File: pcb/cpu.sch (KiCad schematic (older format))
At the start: 35 parts, among them P27 BDM, P57 TX1, P58 RX1, P59 TX, P60 RX, P64 CAN-RX-TX, U1 MC9S12XDP512, X1 16MHz

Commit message: Renamed RX to RX0 and TX to TX0 since there is RX1/TX1 already marked.
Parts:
- P59: value TX -> TX0
- P60: value RX -> RX0
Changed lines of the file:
@@
-EESchema Schematic File Version 2  date Thu 23 May 2013 09:58:23 PM EDT
+EESchema Schematic File Version 2  date Fri 24 May 2013 09:31:09 PM EDT
 LIBS:opto
 LIBS:power
@@
 Sheet 2 7
 Title "Jaguar PCB for FreeEMS"
-Date "24 may 2013"
+Date "25 may 2013"
 Rev "0.6-alpha"
 Comp "git hash: xxxxxxxxxx"
@@
 P 5600 1500
 F 0 "P60" H 5680 1500 40  0000 L CNN
-F 1 "RX" H 5600 1555 30  0001 C CNN
+F 1 "RX0" H 5600 1555 30  0001 C CNN
 	1    5600 1500
 	0    -1   -1   0
@@
 P 5500 1500
 F 0 "P59" H 5580 1500 40  0000 L CNN
-F 1 "TX" H 5500 1555 30  0001 C CNN
+F 1 "TX0" H 5500 1555 30  0001 C CNN
 	1    5500 1500
 	0    -1   -1   0

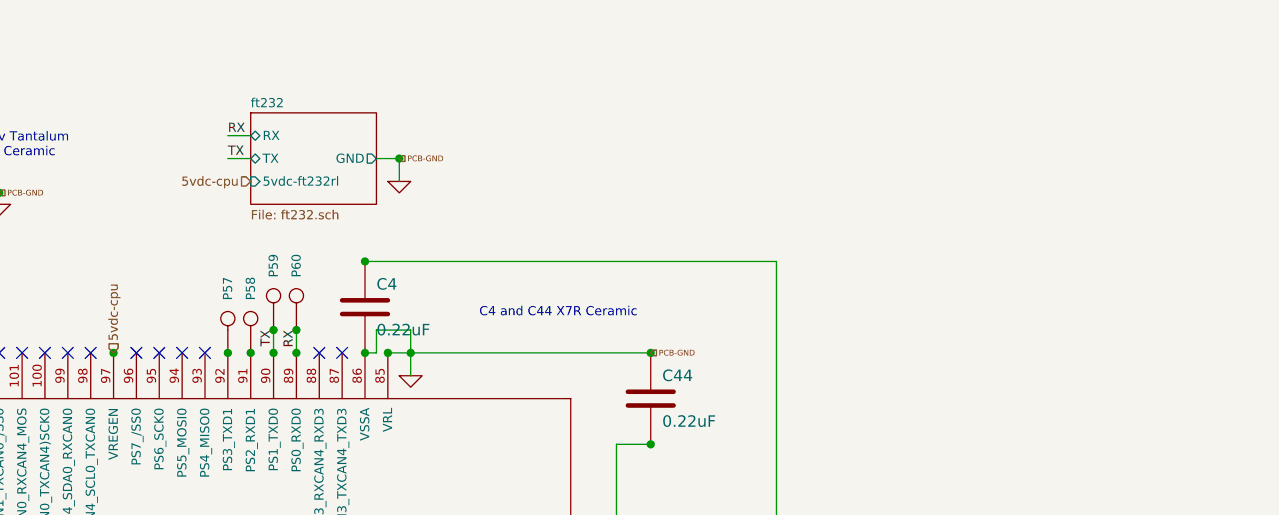
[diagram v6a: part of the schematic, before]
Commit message: Changed RX0/TX0 to a 0.100" 2-pin header for those that want to experiment with TTL serial devices other than the FTDI USB IC.
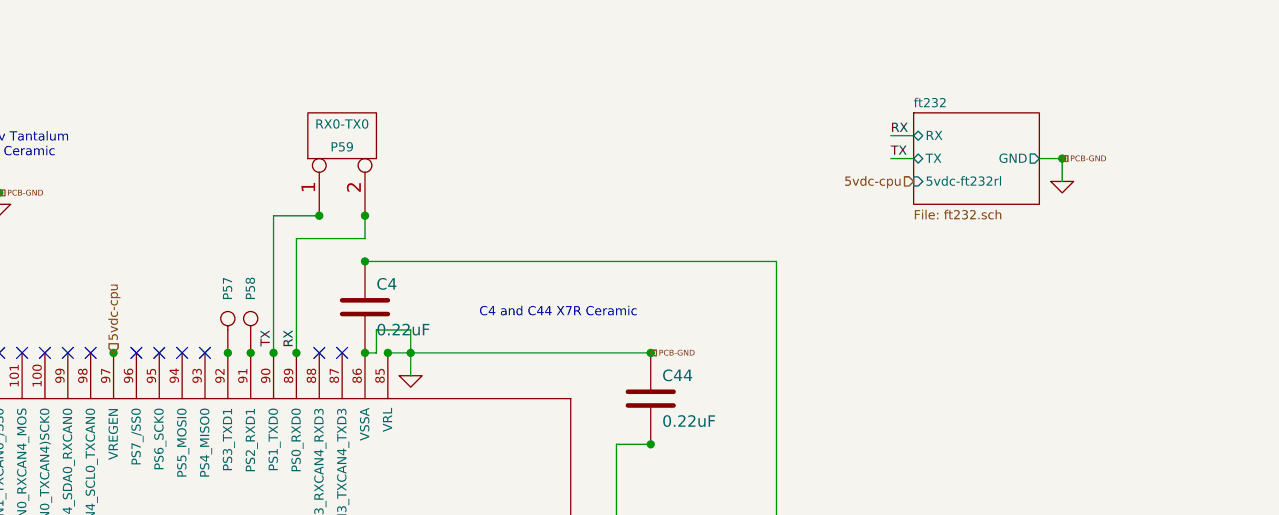
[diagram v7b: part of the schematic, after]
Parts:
- removed P59: TX0, symbol CONN_1
- removed P60: RX0, symbol CONN_1
- added P59: RX0-TX0, symbol CONN_2
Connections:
- wire segments 85 -> 88
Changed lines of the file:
@@
-EESchema Schematic File Version 2  date Fri 24 May 2013 09:46:28 PM EDT
+EESchema Schematic File Version 2  date Fri 24 May 2013 09:53:21 PM EDT
 LIBS:opto
 LIBS:power
@@
 Comment4 ""
 $EndDescr
+Connection ~ 5700 1150
+Connection ~ 5900 1150
+Wire Wire Line
+	5500 1150 5700 1150
+Wire Wire Line
+	5500 1750 5500 1150
 Connection ~ 4200 1650
 Connection ~ 4000 1650
@@
 Wire Wire Line
 	4100 7700 4100 7500
-Connection ~ 6050 900
+Connection ~ 8950 900
 Connection ~ 1700 7000
 Connection ~ 1250 6550
@@
 	7000 2850 7700 2850
 Wire Wire Line
-	6050 1000 6050 900
+	8950 1000 8950 900
 Wire Notes Line
 	2150 6350 2150 7700
@@
 	2200 4050 1450 4050
 Wire Wire Line
-	5500 1750 5500 1650
-Wire Wire Line
-	5400 800  5300 800
+	8300 800  8200 800
 Connection ~ 8400 6350
 Wire Wire Line
-	5400 900  5300 900
-Wire Wire Line
-	5600 1750 5600 1650
+	8300 900  8200 900
 Connection ~ 1600 7050
 Connection ~ 1600 7150
@@
 	1600 7400 1600 7250
 Wire Wire Line
-	6050 900  5950 900
+	8950 900  8850 900
 Wire Wire Line
 	7700 2850 7700 1350
@@
 Connection ~ 5400 1750
 Connection ~ 5300 1750
-Connection ~ 5500 1650
-Connection ~ 5600 1650
 Connection ~ 2200 4450
 Connection ~ 2200 4550
@@
 Wire Wire Line
 	4100 1650 4200 1650
+Wire Wire Line
+	5600 1750 5600 1250
+Wire Wire Line
+	5600 1250 5900 1250
+Wire Wire Line
+	5900 1250 5900 1150
+$Comp
+L CONN_2 P59
+U 1 1 51A0194D
+P 5800 800
+F 0 "P59" V 5750 800 40  0000 C CNN
+F 1 "RX0-TX0" V 5850 800 40  0000 C CNN
+	1    5800 800
+	0    -1   -1   0
+$EndComp
 $Comp
 L CONN_2 P64
@@
 Fan-PK4
 $Comp
-L CONN_1 P60
-U 1 1 505D2CE4
-P 5600 1500
-F 0 "P60" H 5680 1500 40  0000 L CNN
-F 1 "RX0" H 5600 1555 30  0001 C CNN
-	1    5600 1500
-	0    -1   -1   0
-$EndComp
-$Comp
-L CONN_1 P59
-U 1 1 505D2CDB
-P 5500 1500
-F 0 "P59" H 5580 1500 40  0000 L CNN
-F 1 "TX0" H 5500 1555 30  0001 C CNN
-	1    5500 1500
-	0    -1   -1   0
-$EndComp
-$Comp
 L CONN_1 P57
 U 1 1 505D24DB
@@
 Text HLabel 7150 1750 2    25   Input ~ 0
 PCB-GND
-Text HLabel 6050 900  2    25   Input ~ 0
+Text HLabel 8950 900  2    25   Input ~ 0
 PCB-GND
 Text HLabel 4300 1050 2    25   Input ~ 0
@@
 Text HLabel 3800 7500 0    40   Input ~ 0
 5vdc-cpu
-Text HLabel 5400 1000 0    40   Input ~ 0
+Text HLabel 8300 1000 0    40   Input ~ 0
 5vdc-cpu
 $Comp
@@
 L GND #PWR08
 U 1 1 4F1C287C
-P 6050 1000
-F 0 "#PWR08" H 6050 1000 30  0001 C CNN
-F 1 "GND" H 6050 930 30  0001 C CNN
-	1    6050 1000
+P 8950 1000
+F 0 "#PWR08" H 8950 1000 30  0001 C CNN
+F 1 "GND" H 8950 930 30  0001 C CNN
+	1    8950 1000
 	1    0    0    -1
 $EndComp
@@
 NoConn ~ 4700 1750
 $Sheet
-S 5400 700  550  400
+S 8300 700  550  400
 U 4F0A3F95
 F0 "ft232" 40
 F1 "ft232.sch" 40
-F2 "RX" B L 5400 800 40
-F3 "TX" B L 5400 900 40
-F4 "GND" O R 5950 900 40
-F5 "5vdc-ft232rl" I L 5400 1000 40
+F2 "RX" B L 8300 800 40
+F3 "TX" B L 8300 900 40
+F4 "GND" O R 8850 900 40
+F5 "5vdc-ft232rl" I L 8300 1000 40
 $EndSheet
 NoConn ~ 2200 3250
@@
 	-1   0    0    1
 $EndComp
-Text Label 5300 900  0    40   ~ 0
+Text Label 8200 900  0    40   ~ 0
 TX
-Text Label 5300 800  0    40   ~ 0
+Text Label 8200 800  0    40   ~ 0
 RX
 Text Label 5600 1650 3    40   ~ 0

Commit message: Removed polyswitch_smd library as it isn't needed after I changed F1 component to a different type to match F2.
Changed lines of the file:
@@
-EESchema Schematic File Version 2  date Fri 24 May 2013 09:53:21 PM EDT
+EESchema Schematic File Version 2  date Wed 29 May 2013 06:21:31 PM EDT
 LIBS:opto
 LIBS:power
 LIBS:conn
 LIBS:transistors
-LIBS:polyswitch_smd
 LIBS:device
 LIBS:Jaguar
@@
 Sheet 2 7
 Title "Jaguar PCB for FreeEMS"
-Date "25 may 2013"
+Date "29 may 2013"
 Rev "0.6-alpha"
 Comp "git hash: xxxxxxxxxx"
@@
 Connection ~ 5900 1150
 Wire Wire Line
-	5500 1150 5700 1150
+	5700 1150 5500 1150
 Wire Wire Line
-	5500 1750 5500 1150
+	5500 1150 5500 1750
 Connection ~ 4200 1650
 Connection ~ 4000 1650
